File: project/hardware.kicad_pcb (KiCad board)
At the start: 4 copper layers, 91 x 106.5 mm, 70 parts, among them IC1 ESP32-S3-MINI-1-N8, IC2 STM32L052K8T6, J1 Conn_01x02_Socket, J2 USB-C, J3 Conn_01x04, J3 ST-Link, J4 Display_OLed, J5 Dig_OUTs, Q1 pnp TO-92 BC307, Q2 pnp TO-92 BC307, Q3 pnp TO-92 BC307, Q4 pnp TO-92 BC307, U1 USBLC6-2SC6, U2 TPS563200, Y1 ABS07-166-32.768KHZ-T, Y2 ECS-400-10-36B2-CKM-TR

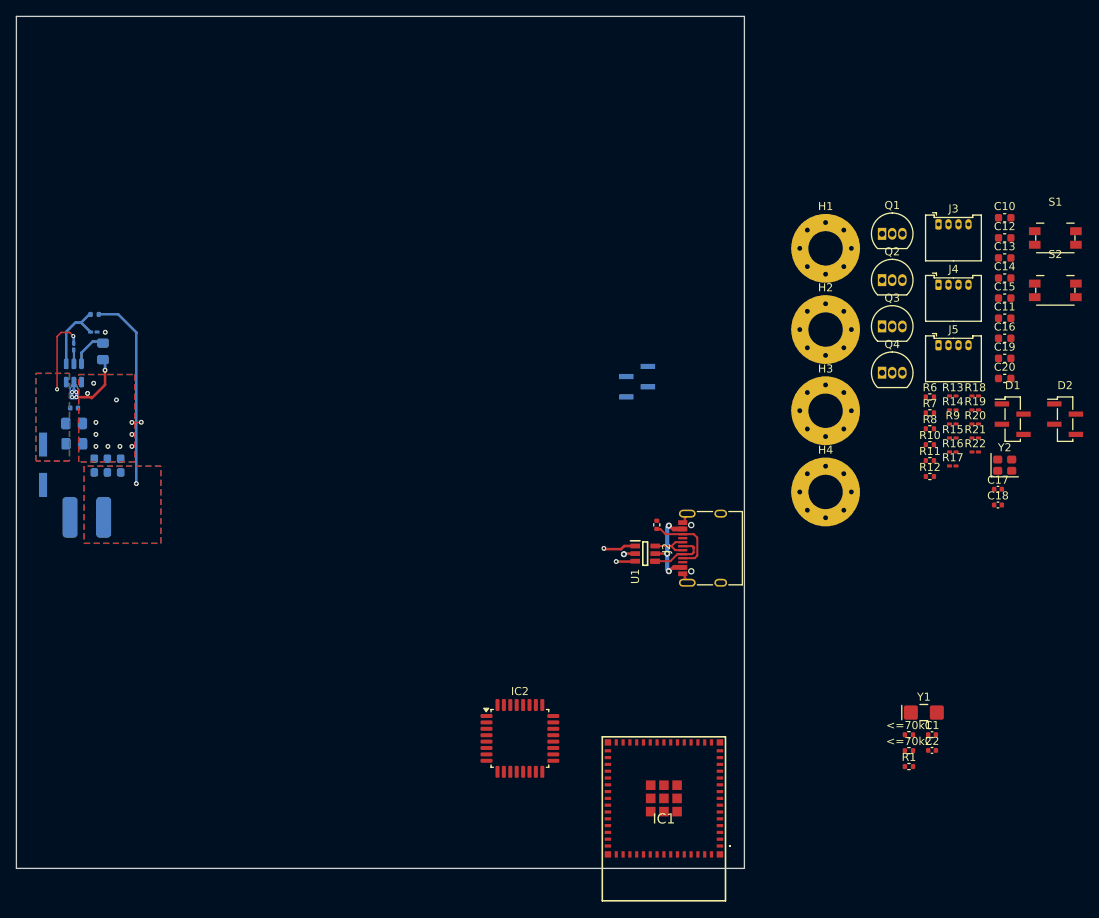
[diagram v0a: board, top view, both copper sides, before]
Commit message: load switch e esp_ready status
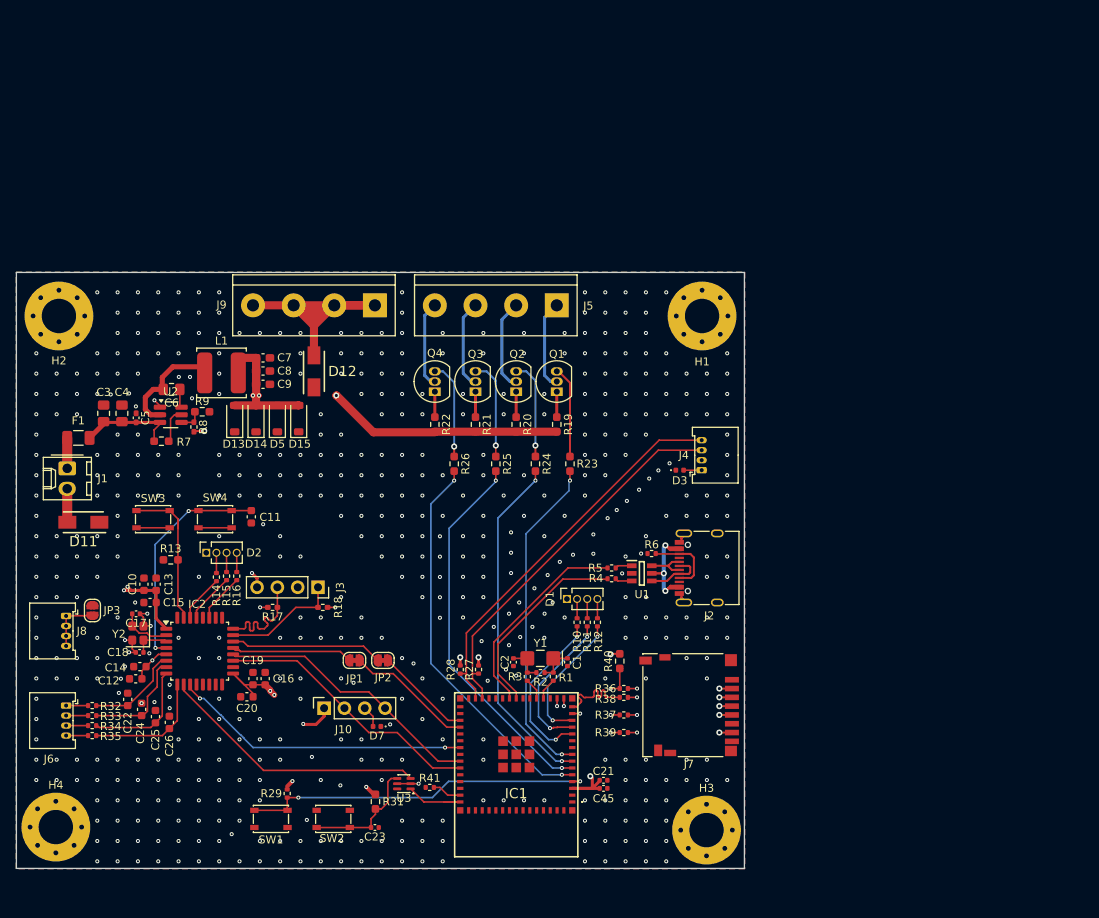
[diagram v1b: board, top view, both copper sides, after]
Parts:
- removed <=70k1, <=70k2: ESR, Resistor_SMD:R_0402_1005Metric
- removed ?: , 
- removed the J3 at (183.7, 76.4)
- removed S1, S2: btSwitch, Button_Switch_SMD:Panasonic_EVQPUK_EVQPUB
- added C21: 22uF, Capacitor_SMD:C_0402_1005Metric, F.Cu at (179.5, 126.2)
- added C22: 7pF, Capacitor_SMD:C_0603_1608Metric, F.Cu at (120.0, 116.1)
- added C23: 100nF, Capacitor_SMD:C_0402_1005Metric, F.Cu at (150.9, 132.1)
- added C24: 7pF, Capacitor_SMD:C_0603_1608Metric, F.Cu at (121.7, 117.4)
- added C25: 7pF, Capacitor_SMD:C_0603_1608Metric, F.Cu at (123.4, 118.3)
- added C26: 7pF, Capacitor_SMD:C_0603_1608Metric, F.Cu at (125.2, 119.0)
- added C45: 100nF, Capacitor_SMD:C_0402_1005Metric, F.Cu at (179.5, 127.2)
- added D11: RB058L-30DDTE25, Project_Library:DIOM5026X220N, F.Cu at (114.4, 94.0)
- added D12: RB058L-30DDTE25, Project_Library:DIOM5026X220N, F.Cu at (143.3, 75.1)
- added D13: D_Zener_Filled, Diode_SMD:D_SOD-123, F.Cu at (133.3, 81.0)
- added D14: D_Zener_Filled, Diode_SMD:D_SOD-123, F.Cu at (136.0, 81.0)
- added D15: D_Zener_Filled, Diode_SMD:D_SOD-123, F.Cu at (141.4, 81.0)
- added D3: CDBQR42/43-HF, Diode_SMD:D_0402_1005Metric, F.Cu at (189.0, 87.5)
- added D5: D_Zener_Filled, Diode_SMD:D_SOD-123, F.Cu at (138.7, 81.0)
- added D7: CDBQR42/43-HF, Diode_SMD:D_0402_1005Metric, F.Cu at (151.1, 119.5)
- added F1: Fuse_Small, Fuse:Fuse_1206_3216Metric, F.Cu at (113.8, 83.4)
- added J10: UART, Connector_PinSocket_2.54mm:PinSocket_1x04_P2.54mm_Vertical, F.Cu at (144.5, 117.2)
- added J6: Analog_INs, Connector_Molex:Molex_PicoBlade_53048-0410_1x04_P1.25mm_Horizontal, F.Cu at (112.3, 116.9)
- added J7: 798-DM3D-SF, Connector_Card:microSD_HC_Hirose_DM3D-SF, F.Cu at (190.2, 116.8)
- added J8: Analog_INs, Connector_Molex:Molex_PicoBlade_53048-0410_1x04_P1.25mm_Horizontal, F.Cu at (112.3, 105.7)
- added J9: Dig_OUTs, TerminalBlock:TerminalBlock_bornier-4_P5.08mm, F.Cu at (150.9, 66.9)
- added JP1: SolderJumper_2_Bridged, Jumper:SolderJumper-2_P1.3mm_Bridged_RoundedPad1.0x1.5mm, F.Cu at (148.3, 111.3)
- added JP2: SolderJumper_2_Bridged, Jumper:SolderJumper-2_P1.3mm_Bridged_RoundedPad1.0x1.5mm, F.Cu at (151.9, 111.3)
- added JP3: SolderJumper_2_Open, Jumper:SolderJumper-2_P1.3mm_Open_RoundedPad1.0x1.5mm, F.Cu at (115.6, 105.0)
- added R23: SMD R, Resistor_SMD:R_0603_1608Metric_Pad0.98x0.95mm_HandSolder, F.Cu at (175.3, 86.7)
- added R24: SMD R, Resistor_SMD:R_0603_1608Metric_Pad0.98x0.95mm_HandSolder, F.Cu at (170.9, 86.7)
- added R25: SMD R, Resistor_SMD:R_0603_1608Metric_Pad0.98x0.95mm_HandSolder, F.Cu at (166.0, 86.7)
- added R26: SMD R, Resistor_SMD:R_0603_1608Metric_Pad0.98x0.95mm_HandSolder, F.Cu at (160.8, 86.7)
- added R27: 1K, Resistor_SMD:R_0402_1005Metric, F.Cu at (163.8, 112.4)
- added R28: 1K, Resistor_SMD:R_0402_1005Metric, F.Cu at (161.5, 112.4)
- added R29: 10K, Resistor_SMD:R_0402_1005Metric, F.Cu at (139.9, 127.9)
- added R31: 10K, Resistor_SMD:R_0603_1608Metric_Pad0.98x0.95mm_HandSolder, F.Cu at (150.9, 128.9)
- added R32: R, Resistor_SMD:R_0402_1005Metric, F.Cu at (115.5, 116.9)
- added R33: R, Resistor_SMD:R_0402_1005Metric, F.Cu at (115.5, 118.2)
- added R34: R, Resistor_SMD:R_0402_1005Metric, F.Cu at (115.5, 119.4)
- added R35: R, Resistor_SMD:R_0402_1005Metric, F.Cu at (115.5, 120.7)
- added R36: 49.9K, Resistor_SMD:R_0402_1005Metric, F.Cu at (182.0, 114.8)
- added R37: 49.9K, Resistor_SMD:R_0402_1005Metric, F.Cu at (182.0, 118.1)
- added R38: 49.9K, Resistor_SMD:R_0402_1005Metric, F.Cu at (182.0, 115.9)
- added R39: 49.9K, Resistor_SMD:R_0402_1005Metric, F.Cu at (182.0, 120.3)
- added R40: 10kR, Resistor_SMD:R_0603_1608Metric_Pad0.98x0.95mm_HandSolder, F.Cu at (181.5, 111.3)
- added R41: 1K, Resistor_SMD:R_0402_1005Metric, F.Cu at (157.7, 127.1)
- added SW1: SW_Push, Button_Switch_SMD:SW_SPST_PTS810, F.Cu at (137.9, 131.1)
- added SW2: SW_Push, Button_Switch_SMD:SW_SPST_PTS810, F.Cu at (145.7, 131.1)
- added SW3: SW_Push, Button_Switch_SMD:SW_SPST_PTS810, F.Cu at (123.1, 93.6)
- added SW4: SW_Push, Button_Switch_SMD:SW_SPST_PTS810, F.Cu at (130.9, 93.6)
- added U3: SiP32431DR3, Package_TO_SOT_SMD:SOT-363_SC-70-6, F.Cu at (154.5, 126.7)
- C1, C2: value TBD -> 12pF
- C3, C4, C6, C7, C8, C9, L1: moved to F.Cu
- C5: footprint Capacitor_SMD:C_0402_1005Metric -> Capacitor_SMD:C_0402_1005Metric_Pad0.74x0.62mm_HandSolder; moved to F.Cu
- D1, D2: footprint Connector_PinSocket_1.27mm:PinSocket_1x04_P1.27mm_Vertical_SMD_Pin1Left -> Connector_PinSocket_1.27mm:PinSocket_1x04_P1.27mm_Vertical
- J1: footprint Connector_PinSocket_2.54mm:PinSocket_2x01_P2.54mm_Vertical_SMD -> Connector_Molex:Molex_KK-254_AE-6410-02A_1x02_P2.54mm_Vertical; moved to F.Cu
- J3: footprint Connector_Molex:Molex_PicoBlade_53048-0410_1x04_P1.25mm_Horizontal -> Connector_PinSocket_2.54mm:PinSocket_1x04_P2.54mm_Vertical
- J5: footprint Connector_Molex:Molex_PicoBlade_53048-0410_1x04_P1.25mm_Horizontal -> TerminalBlock:TerminalBlock_bornier-4_P5.08mm
- R1: value TBD -> 0R
- R13: value 1K -> 10kR; footprint Resistor_SMD:R_0201_0603Metric_Pad0.64x0.40mm_HandSolder -> Resistor_SMD:R_0603_1608Metric_Pad0.98x0.95mm_HandSolder
- R14: value 1K -> 560R; footprint Resistor_SMD:R_0201_0603Metric_Pad0.64x0.40mm_HandSolder -> Resistor_SMD:R_0402_1005Metric
- R15, R16: value SMD R -> 560R; footprint Resistor_SMD:R_0201_0603Metric_Pad0.64x0.40mm_HandSolder -> Resistor_SMD:R_0402_1005Metric
- R17, R18: value SMD R -> 1K; footprint Resistor_SMD:R_0201_0603Metric_Pad0.64x0.40mm_HandSolder -> Resistor_SMD:R_0402_1005Metric_Pad0.72x0.64mm_HandSolder
- R19, R20, R21, R22: footprint Resistor_SMD:R_0201_0603Metric_Pad0.64x0.40mm_HandSolder -> Resistor_SMD:R_0603_1608Metric_Pad0.98x0.95mm_HandSolder
- R2: value 5K1 -> TBD
- R3, R5: value 10K -> 0R; footprint Resistor_SMD:R_0201_0603Metric_Pad0.64x0.40mm_HandSolder -> Resistor_SMD:R_0402_1005Metric; moved to F.Cu
- R4: value 33.2K -> 0R; moved to F.Cu
- R6: value 560R -> 5K1
- R7: value 560R -> 10K; footprint Resistor_SMD:R_0402_1005Metric -> Resistor_SMD:R_0603_1608Metric_Pad0.98x0.95mm_HandSolder
- R8: value 560R -> 33.2K; footprint Resistor_SMD:R_0402_1005Metric -> Resistor_SMD:R_0402_1005Metric_Pad0.72x0.64mm_HandSolder
- R9: value 10kR -> 10K; footprint Resistor_SMD:R_0201_0603Metric_Pad0.64x0.40mm_HandSolder -> Resistor_SMD:R_0603_1608Metric_Pad0.98x0.95mm_HandSolder
- U2: footprint Package_TO_SOT_SMD:SOT-23-6 -> Package_TO_SOT_SMD:SOT-23-6_Handsoldering; moved to F.Cu
- moved C12 121.8 mm to (121.0, 113.6), turned to 180 degrees
- moved C14 118.5 mm to (121.5, 112.0), turned to 180 degrees
- moved C10 116.9 mm to (122.0, 101.7), turned to 90 degrees
- moved C13 113.6 mm to (123.5, 101.7), turned to 90 degrees
- moved C15 113.4 mm to (122.8, 104.0), turned to 180 degrees
- moved Y2 110.4 mm to (121.2, 107.8), turned to 90 degrees
- moved C18 108.9 mm to (121.5, 110.3), turned to 180 degrees
- moved C17 108.9 mm to (121.0, 105.4), turned to 180 degrees
- moved D2 108.6 mm to (129.8, 97.8), turned to 90 degrees
- moved H4 104.9 mm to (111.0, 132.1)
- moved C20 102.7 mm to (134.9, 115.8), turned to 180 degrees
- moved C19 102.1 mm to (135.6, 113.5), turned to 90 degrees
- moved C16 101.8 mm to (137.2, 113.5), turned to 90 degrees
- moved R13 99.9 mm to (125.3, 98.7), turned to 180 degrees
- moved C11 97.4 mm to (135.4, 93.3), turned to 90 degrees
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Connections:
- net CLK_IN renamed CLK_STM_IN
- net CLK_OUT renamed CLK_STM_OUT
- net Net-(J5-GND) renamed /DO_1
- net Net-(J5-SCL) renamed /DO_3
- net Net-(J5-SDA) renamed /DO_4
- net Net-(J5-VCC) renamed /DO_2
- C1 pad 2: Net-(<=70k1-Pad1) -> Net-(C1-Pad2)
- C10 pad 1: VDD -> 3V3
- C12 pad 1: VDA -> 3V3
- C13 pad 1: VDD -> 3V3
- C14 pad 1: VDA -> 3V3
- C15 pad 1: VDD -> 3V3
- C16 pad 1: VDD -> 3V3
- C19 pad 1: VDD -> 3V3
- C2 pad 1: Net-(<=70k2-Pad1) -> Net-(C2-Pad1)
- C20 pad 1: VDD -> 3V3
- C3 pad 1: GND_E -> GND
- C3 pad 2: 12 -> +12V
- C4 pad 1: GND_E -> GND
- C4 pad 2: 12 -> +12V
- C5 pad 1: GND_E -> GND
- C5 pad 2: 12 -> +12V
- C7 pad 1: GND_E -> GND
- C8 pad 1: GND_E -> GND
- C9 pad 1: GND_E -> GND
- D1 pad 1: GND_E -> GND
- D2 pad 1: GND_E -> GND
- IC1 pad 1: unconnected-(IC1-GND_1-Pad1) -> GND
- IC1 pad 11: unconnected-(IC1-IO7-Pad11) -> LED_ESP_R
- IC1 pad 12: unconnected-(IC1-IO8-Pad12) -> LED_ESP_G
- IC1 pad 13: unconnected-(IC1-IO9-Pad13) -> LED_ESP_B
- IC1 pad 14: unconnected-(IC1-IO10-Pad14) -> uCHIP_CS
- IC1 pad 15: unconnected-(IC1-IO11-Pad15) -> uCHIP_DI
- IC1 pad 16: unconnected-(IC1-IO12-Pad16) -> uCHIP_SCK
- IC1 pad 17: unconnected-(IC1-IO13-Pad17) -> uCHIP_DO
- IC1 pad 19: Net-(IC1-IO15) -> CLK_ESP_1
- IC1 pad 2: unconnected-(IC1-GND_2-Pad2) -> GND
- IC1 pad 20: Net-(IC1-IO16) -> CLK_ESP_2
- IC1 pad 23: unconnected-(IC1-IO19-Pad23) -> Net-(IC1-IO19)
- IC1 pad 24: unconnected-(IC1-IO20-Pad24) -> Net-(IC1-IO20)
- IC1 pad 28: unconnected-(IC1-IO33-Pad28) -> Dp_SDA
- IC1 pad 29: unconnected-(IC1-IO34-Pad29) -> Dp_SCL
- IC1 pad 3: unconnected-(IC1-3V3-Pad3) -> 3V3
- IC1 pad 33: unconnected-(IC1-IO37-Pad33) -> Net-(IC1-IO37)
- IC1 pad 34: unconnected-(IC1-IO38-Pad34) -> Net-(IC1-IO38)
- IC1 pad 37: unconnected-(IC1-IO41-Pad37) -> ESP_READY
- IC1 pad 39: unconnected-(IC1-TXD0-Pad39) -> RX_1
- IC1 pad 4: unconnected-(IC1-IO0-Pad4) -> BOOT
- IC1 pad 40: unconnected-(IC1-RXD0-Pad40) -> RX_0
- IC1 pad 42: unconnected-(IC1-GND_3-Pad42) -> GND
- IC1 pad 43: unconnected-(IC1-GND_4-Pad43) -> GND
- IC1 pad 44: unconnected-(IC1-IO46-Pad44) -> GPIO_46
- IC1 pad 45: unconnected-(IC1-EN-Pad45) -> EN
- IC1 pad 46: unconnected-(IC1-GND_5-Pad46) -> GND
- IC1 pad 47: unconnected-(IC1-GND_6-Pad47) -> GND
- IC1 pad 48: unconnected-(IC1-GND_7-Pad48) -> GND
- IC1 pad 49: unconnected-(IC1-GND_8-Pad49) -> GND
- IC1 pad 5: unconnected-(IC1-IO1-Pad5) -> digOut_pin_4
- IC1 pad 50: unconnected-(IC1-GND_9-Pad50) -> GND
- IC1 pad 51: unconnected-(IC1-GND_10-Pad51) -> GND
- IC1 pad 52: unconnected-(IC1-GND_11-Pad52) -> GND
- IC1 pad 53: unconnected-(IC1-GND_12-Pad53) -> GND
- IC1 pad 54: unconnected-(IC1-GND_13-Pad54) -> GND
- IC1 pad 55: unconnected-(IC1-GND_14-Pad55) -> GND
- IC1 pad 56: unconnected-(IC1-GND_15-Pad56) -> GND
- IC1 pad 57: unconnected-(IC1-GND_16-Pad57) -> GND
- IC1 pad 58: unconnected-(IC1-GND_17-Pad58) -> GND
- IC1 pad 59: unconnected-(IC1-GND_18-Pad59) -> GND
- IC1 pad 6: unconnected-(IC1-IO2-Pad6) -> digOut_pin_3
- IC1 pad 60: unconnected-(IC1-GND_19-Pad60) -> GND
- IC1 pad 61: unconnected-(IC1-GND_20-Pad61) -> GND
- IC1 pad 62: unconnected-(IC1-GND_21-Pad62) -> GND
- IC1 pad 63: unconnected-(IC1-GND_22-Pad63) -> GND
- IC1 pad 64: unconnected-(IC1-GND_23-Pad64) -> GND
- IC1 pad 65: unconnected-(IC1-GND_24-Pad65) -> GND
- IC1 pad 66: unconnected-(IC1-GND_25-Pad66) -> GND
- IC1 pad 67: unconnected-(IC1-GND_26-Pad67) -> GND
- IC1 pad 68: unconnected-(IC1-GND_27-Pad68) -> GND
- IC1 pad 69: unconnected-(IC1-GND_28-Pad69) -> GND
- IC1 pad 7: unconnected-(IC1-IO3-Pad7) -> digOut_pin_2
- IC1 pad 70: unconnected-(IC1-GND_29-Pad70) -> GND
- IC1 pad 71: unconnected-(IC1-GND_30-Pad71) -> GND
- IC1 pad 72: unconnected-(IC1-GND_31-Pad72) -> GND
- IC1 pad 73: unconnected-(IC1-GND_32-Pad73) -> GND
- IC1 pad 8: unconnected-(IC1-IO4-Pad8) -> digOut_pin_1
- IC2 pad 1: VDD -> 3V3
- IC2 pad 10: unconnected-(IC2-PA4-Pad10) -> ESP_EN
- IC2 pad 11: unconnected-(IC2-PA5-Pad11) -> ESP_READY
- IC2 pad 17: VDD -> 3V3
- IC2 pad 19: UART_TX -> RX_0
- IC2 pad 20: UART_RX -> RX_1
- IC2 pad 21: unconnected-(IC2-PA11-Pad21) -> CTS_1
- IC2 pad 22: unconnected-(IC2-PA12-Pad22) -> CTS_0
- IC2 pad 27: unconnected-(IC2-PB4-Pad27) -> LED_STM_B
- IC2 pad 29: unconnected-(IC2-PB6-Pad29) -> LED_STM_G
- IC2 pad 30: unconnected-(IC2-PB7-Pad30) -> LED_STM_R
- IC2 pad 5: VDA -> 3V3
- IC2 pad 6: unconnected-(IC2-PA0-Pad6) -> AIN_pin_1
- IC2 pad 7: unconnected-(IC2-PA1-Pad7) -> AIN_pin_2
- IC2 pad 8: unconnected-(IC2-PA2-Pad8) -> AIN_pin_3
- IC2 pad 9: unconnected-(IC2-PA3-Pad9) -> AIN_pin_4
- J1 pad 1: 12 -> Net-(J1-Pin_1)
- J1 pad 2: GND_E -> Net-(D11-A)
- J3 pad 4: VDD -> 3V3
- J4 pad 1: GND -> Net-(D3-A)
- J4 pad 2: VDD -> 3V3
- J4 pad 3: Dp_SCL -> Dp_SDA
- J4 pad 4: Dp_SDA -> Dp_SCL
- R1 pad 1: Net-(<=70k1-Pad1) -> CLK_ESP_1
- R1 pad 2: Net-(<=70k2-Pad1) -> Net-(C1-Pad2)
- R10 pad 1: LED_STM_R -> LED_ESP_R
- R10 pad 2: Net-(D2-RK) -> Net-(D1-RK)
- R11 pad 1: LED_STM_G -> LED_ESP_G
- R11 pad 2: Net-(D2-GK) -> Net-(D1-GK)
- R12 pad 1: LED_STM_B -> LED_ESP_B
- R12 pad 2: Net-(D2-BK) -> Net-(D1-BK)
- R13 pad 1: ST_SCL -> BOOT0
- R13 pad 2: VDD -> GND
- R14 pad 1: ST_SDA -> LED_STM_R
- R14 pad 2: VDD -> Net-(D2-RK)
- R15 pad 1: Net-(Q1-C) -> LED_STM_G
- R15 pad 2: VDD -> Net-(D2-GK)
- R16 pad 1: Net-(Q2-C) -> LED_STM_B
- R16 pad 2: VDD -> Net-(D2-BK)
- R17 pad 1: Net-(Q3-C) -> ST_SCL
- R17 pad 2: VDD -> 3V3
- R18 pad 1: Net-(Q4-C) -> ST_SDA
- R18 pad 2: VDD -> 3V3
- R19 pad 1: Net-(Q1-B) -> Net-(Q1-C)
- R19 pad 2: digOut_pin_1 -> 3V3
- R2 pad 1: /CC1 -> Net-(C1-Pad2)
- R2 pad 2: GND -> Net-(C2-Pad1)
- R20 pad 1: Net-(Q2-B) -> Net-(Q2-C)
- R20 pad 2: digOut_pin_2 -> 3V3
- R21 pad 1: Net-(Q3-B) -> Net-(Q3-C)
- R21 pad 2: digOut_pin_3 -> 3V3
- R22 pad 1: Net-(Q4-B) -> Net-(Q4-C)
- R22 pad 2: digOut_pin_4 -> 3V3
- R3 pad 1: 12 -> CLK_ESP_2
- R3 pad 2: Net-(U2-EN) -> Net-(C2-Pad1)
- R4 pad 1: Net-(U2-VFB) -> Net-(IC1-IO19)
- R4 pad 2: 3V3 -> USB_DN
- R5 pad 1: GND_E -> Net-(IC1-IO20)
- R5 pad 2: Net-(U2-VFB) -> USB_DP
- R6 pad 1: LED_ESP_R -> /CC1
- R6 pad 2: Net-(D1-RK) -> GND
- R7 pad 1: LED_ESP_G -> +12V
- R7 pad 2: Net-(D1-GK) -> Net-(U2-EN)
- R8 pad 1: LED_ESP_B -> Net-(U2-VFB)
- R8 pad 2: Net-(D1-BK) -> 3V3
- R9 pad 1: BOOT0 -> GND
- R9 pad 2: GND -> Net-(U2-VFB)
- U2 pad 1: GND_E -> GND
- U2 pad 3: 12 -> +12V
- Y1 pad 1: Net-(<=70k1-Pad1) -> Net-(C1-Pad2)
- Y1 pad 2: Net-(<=70k2-Pad1) -> Net-(C2-Pad1)
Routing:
- net 3V3: track 24.5 -> 346.6 mm, vias 1 -> 20
- net Dp_SCL: track 0.00 -> 48.8 mm
- net digOut_pin_4: track 0.00 -> 48.7 mm, vias 0 -> 2
- net Dp_SDA: track 0.00 -> 47.3 mm
- net digOut_pin_3: track 0.00 -> 47.2 mm, vias 0 -> 2
- net BOOT: track 0.00 -> 44.2 mm, vias 0 -> 2
- net digOut_pin_2: track 0.00 -> 43.3 mm, vias 0 -> 2
- net digOut_pin_1: track 0.00 -> 40.9 mm, vias 0 -> 2
- net ESP_READY: track 0.00 -> 37.4 mm, vias 0 -> 2
- net RX_0: track 0.00 -> 33.9 mm
- net RX_1: track 0.00 -> 33.9 mm
- net ESP_EN: track 0.00 -> 33.7 mm
- net Net-(D12-A): track 0.00 -> 31.2 mm
- net NRST: track 0.00 -> 28.1 mm, vias 0 -> 2
- net Net-(IC1-IO20): track 0.00 -> 25.9 mm
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- added copper zone on B.Cu, net GND
- added copper zone on F.Cu, net GND
- added copper zone on In1.Cu, net GND
- added copper zone on In2.Cu, net GND
- removed copper zone on B.Cu, net 12
- removed copper zone on F.Cu, net 12
- removed copper zone on B.Cu, net 3V3
- removed copper zone on F.Cu, net 3V3
- removed copper zone on B.Cu, net GND_E
- removed copper zone on F.Cu, net GND_E
- removed copper zone on B.Cu, net Net-(U2-SW)
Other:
- board size 91 x 106.5 mm -> 91 x 74.5 mm
